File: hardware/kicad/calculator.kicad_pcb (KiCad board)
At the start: 2 copper layers, 81.3 x 131.4 mm, 63 parts, among them J1 Jack-DC, J2 AudioJack3_SwitchTR, Q1 BC547, SW1 SW_Push, SW10 SW_Push, SW11 SW_Push, SW12 SW_Push, SW13 SW_Push, SW14 SW_Push, SW15 SW_Push, SW16 SW_Push, SW17 SW_Push, SW18 SW_Push, SW19 SW_Push, SW2 SW_Push, SW20 SW_Push, SW21 SW_Push, SW22 SW_Push, SW23 SW_Push, SW24 SW_Push, SW25 SW_Push, SW26 SW_Push, SW27 SW_Push, SW28 SW_Push, SW29 SW_Push, SW3 SW_Push, SW30 SW_Push, SW31 SW_Push, SW32 SW_Push, SW33 SW_Push, SW34 SW_Push, SW35 SW_Push, SW36 SW_Push, SW37 SW_DIP_x04, SW4 SW_Push, SW5 SW_Push, SW6 SW_Push, SW7 SW_Push, SW8 SW_Push, SW9 SW_Push, U1 Pico, U2 Arduino_Nano_v2.x, U3 TFT

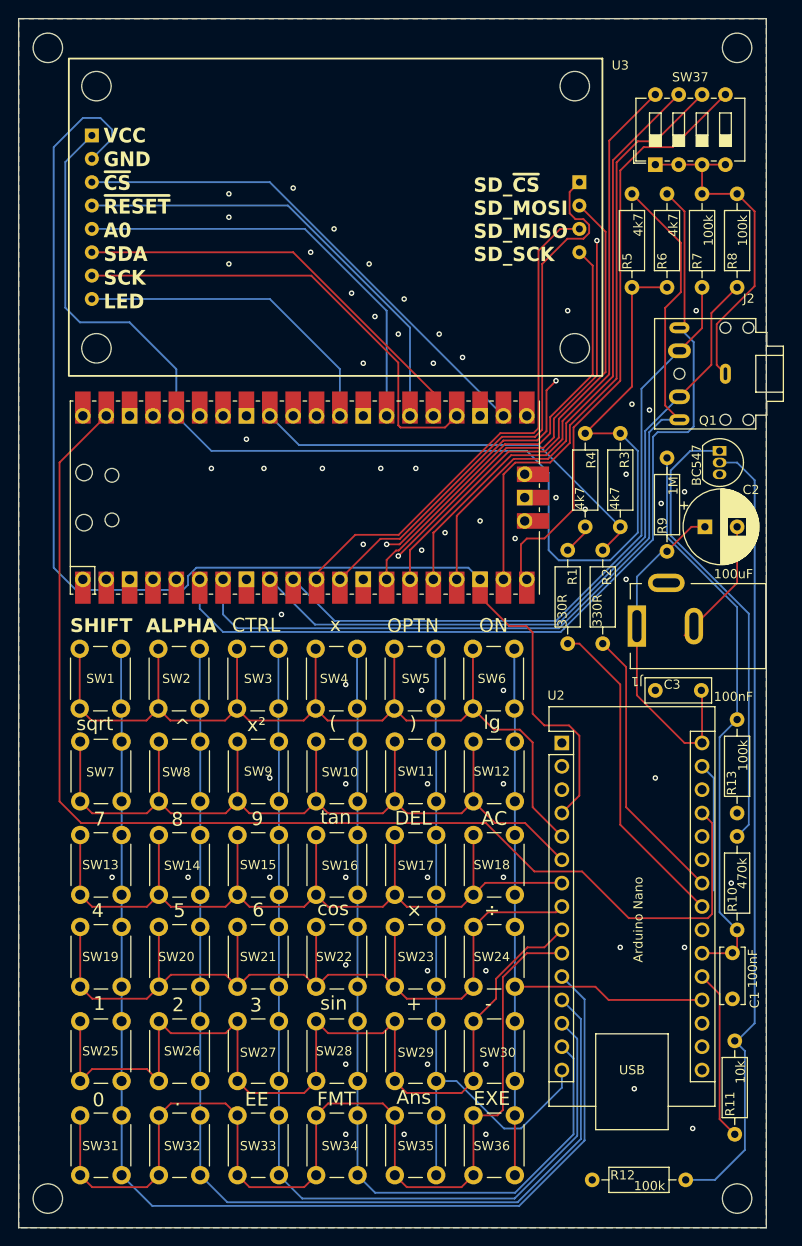
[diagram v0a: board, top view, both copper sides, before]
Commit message: Fix: fatal error in sch & pcb (i2c bus connected to GND) 	修改：     hardware/gerber.zip 	修改：     hardware/kicad/calculator.kicad_pcb 	修改：     hardware/kicad/calculator.kicad_sch 	删除：     hardware/sch.pdf
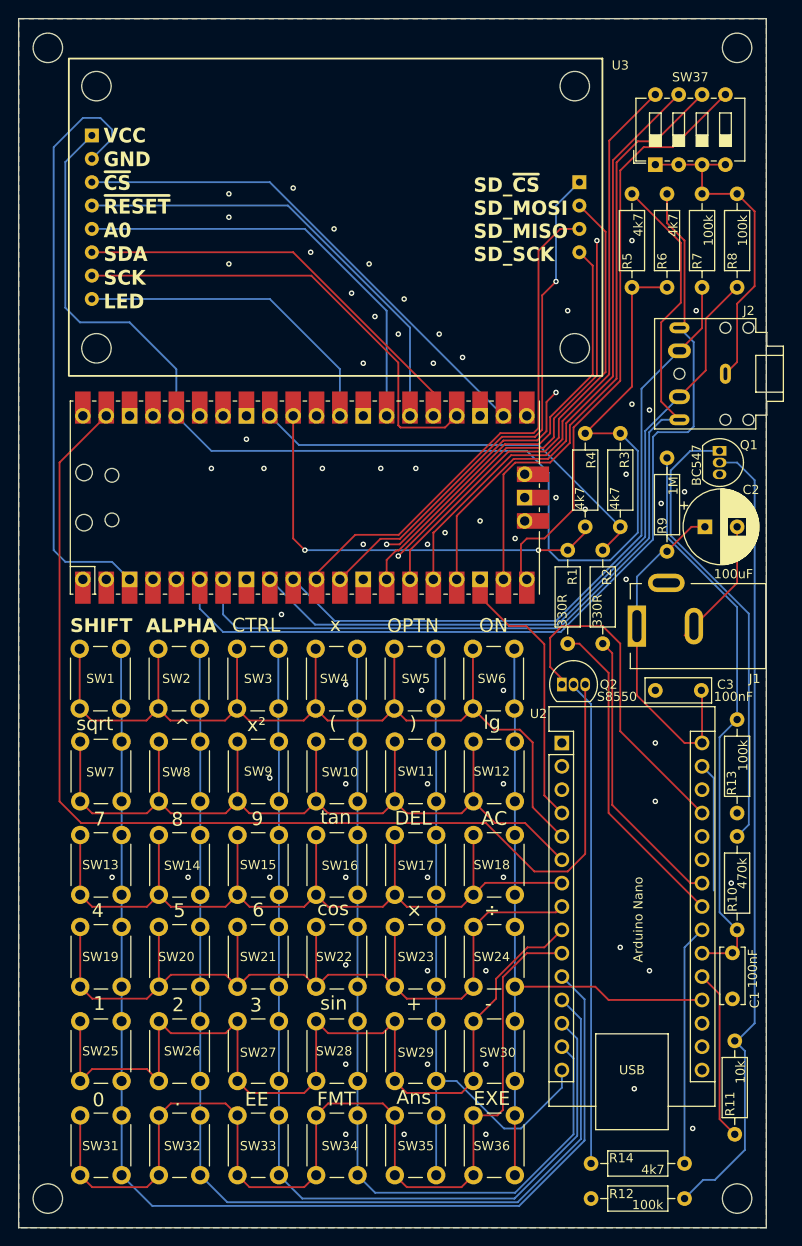
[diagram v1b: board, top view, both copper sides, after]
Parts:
- added Q2: S8550, Package_TO_SOT_THT:TO-92_Inline, F.Cu at (92.7, 96.5)
- added R14: 4k7, Resistor_THT:R_Axial_DIN0207_L6.3mm_D2.5mm_P10.16mm_Horizontal, F.Cu at (95.9, 148.6)
- moved R12 2.04 mm to (106.0, 152.4)
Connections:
- net /Keypad/Col6 renamed /Col6
- net Net-(U2-A1) renamed /A1
- net Net-(U2-A2) renamed /A2
- R1 pad 2: GND -> Net-(U1-GPIO26_ADC0)
- R4 pad 1: GND -> Net-(U1-GPIO26_ADC0)
- U1 pad 31: GND -> Net-(U1-GPIO26_ADC0)
- U1 pad 39: Net-(U1-VSYS) -> Net-(Q2-C)
- U2 pad 22: unconnected-(U2-A3-Pad22) -> /A3
- U2 pad 27: Net-(U1-VSYS) -> +5V
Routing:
- net Net-(U1-VSYS): track 131.8 -> 0.00 mm
- net Net-(Q2-C): track 0.00 -> 123.5 mm
- net Net-(Q2-B): track 0.00 -> 52.9 mm
- net GND: track 283.3 -> 233.0 mm, vias 69 -> 71
- net Net-(U1-GPIO26_ADC0): track 0.00 -> 47.0 mm, vias 0 -> 2
- net +5V: track 0.00 -> 36.6 mm
- net /A3: track 0.00 -> 26.2 mm
- net /_~{SD_CS}: track 60.6 -> 57.3 mm, vias 0 -> 1
- net Net-(Q1-B): track 86.7 -> 87.7 mm
- net Net-(U2-A5): track 30.5 -> 31.3 mm
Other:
- board text added: "S8550"

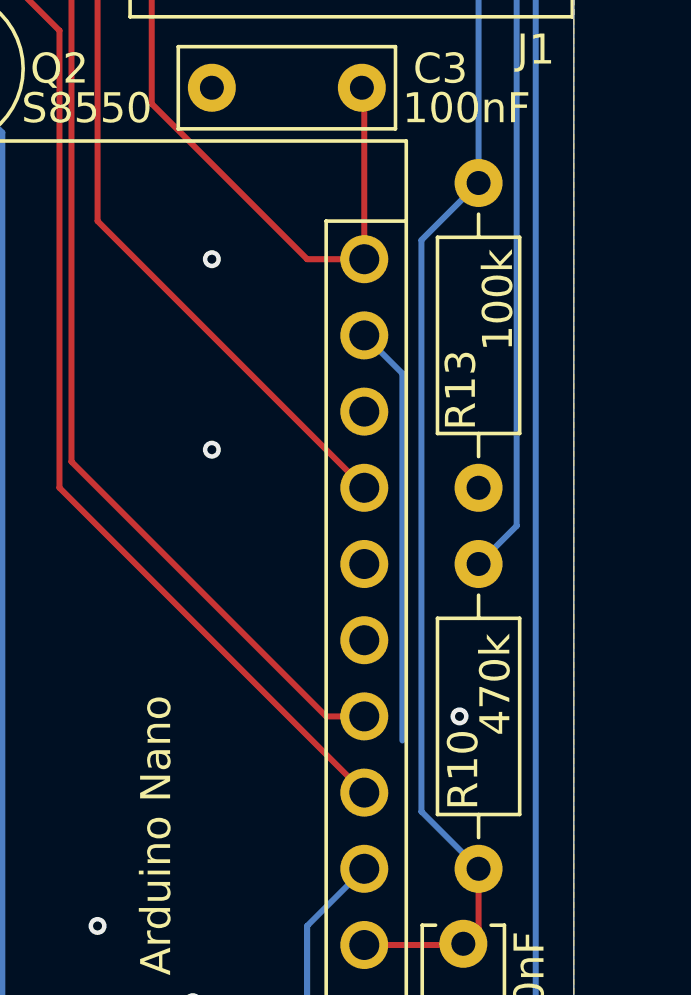
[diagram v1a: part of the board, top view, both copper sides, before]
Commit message: KiCad 10 & 3D 	删除：     hardware/gerber.zip 	新文件：   hardware/gerber260722.zip 	新文件：   "hardware/kicad/AZ-Delivery_18\350\213\261\345\257\270TFT\346\230\276\347\244\272\345\261\217SPI/AZ-Delivery 1.8 inch TFT Display SPI.jpg" 	新文件：   "hardware/kicad/AZ-Delivery_18\350\213\261\345\257\270TFT\346\230\276\347\244\272\345\261\217SPI/AZ-Delivery 1.8 inch TFT Display SPI.pdf" 	新文件：   "hardware/kicad/AZ-Delivery_18\350\213\261\345\257\270TFT\346\230\276\347\244\272\345\261\217SPI/AZ-Delivery 1.8 inch TFT Display SPI.stp" 	新文件：   "hardware/kicad/AZ-Delivery_18\350\213\261\345\257\270TFT\346\230\276\347\244\272\345\261\217SPI/AZ-Delivery 1.8 inch TFT Display SP_2I.jpg" 	新文件：   hardware/kicad/Arduino_Nano/Nano290313.jpg 	新文件：   hardware/kicad/Arduino_Nano/arduino nano.igs 	新文件：   hardware/kicad/Arduino_Nano/arduino nano.step 	新文件：   hardware/kicad/Arduino_Nano/arduino nano290313.zip 	新文件：   hardware/kicad/Arduino_Nano/nano top finised.jpg 	新文件：   hardware/kicad/Arduino_Nano/nano underside2.jpg 	修改：     hardware/kicad/calculator.kicad_pcb 	新文件：   hardware/kicad/calculator.kicad_prl 	修改：     hardware/kicad/calculator.kicad_pro 	新文件：   hardware/kicad/calculator_t.png 	新文件：   hardware/kicad/fp-info-cache 	新文件：   hardware/kicad/fp-lib-table 	修改：     hardware/kicad/keypad.kicad_sch 	新文件：   hardware/kicad/sym-lib-table
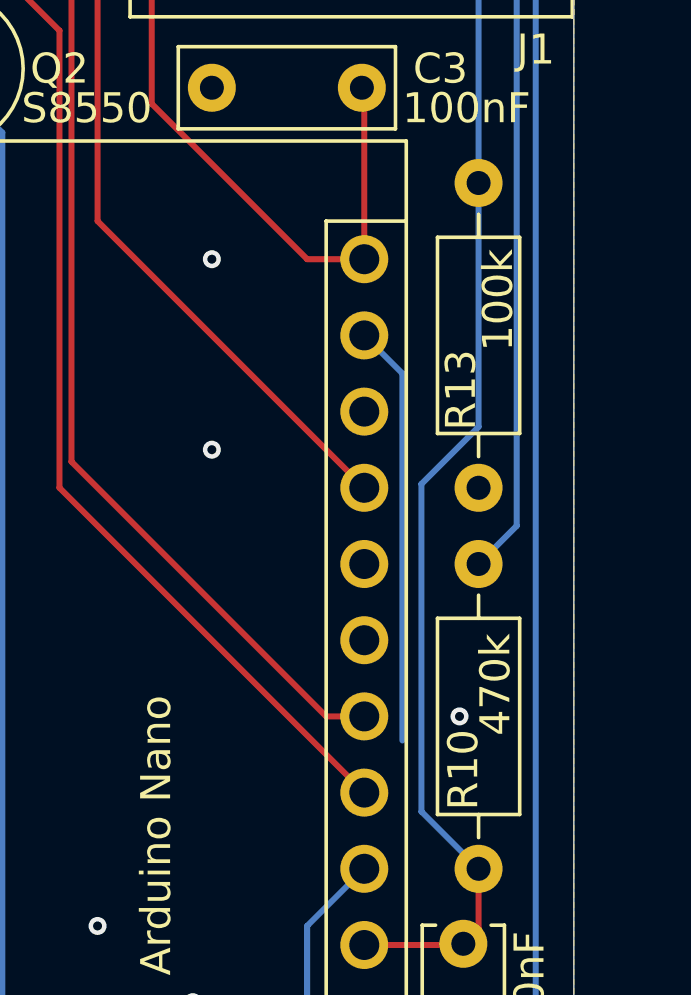
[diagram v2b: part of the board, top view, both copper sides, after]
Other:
- board text added: "Calculator v0.1 {dblquote}Operator Lambda{dblquote}"
- board text added: "Copyright (c) 2026 hdkghc https://github.com/hdkghc/calculator"
- board text removed: "Calculator Version 0.1 Copyright (c) 2026 hdkghc https://github.com/hdkghc/calculator"

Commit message: BJT footprint 	新文件：   hardware/gerber260724.zip 	修改：     hardware/kicad/calculator.kicad_pcb 	修改：     hardware/kicad/calculator.kicad_prl
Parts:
- Q1, Q2: footprint Package_TO_SOT_THT:TO-92_Inline -> Package_TO_SOT_THT:TO-92_Inline_Wide
- moved Q1 3.30 mm to (106.8, 72.4), turned to 0 degrees
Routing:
- net Net-(Q1-C): track 50.0 -> 45.6 mm
- net Net-(Q1-B): track 87.7 -> 86.7 mm
- net Net-(Q2-C): track 123.5 -> 124.4 mm
- net Net-(Q2-B): track 52.9 -> 52.3 mm
